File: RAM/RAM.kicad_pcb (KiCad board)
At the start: 2 copper layers, 138 x 63.8 mm, 52 parts, among them J1 Conn_01x02_Pin, J2 Conn_01x01_Pin, J3 Conn_01x02_Pin, J4 Conn_01x01_Pin, J5 Conn_01x05_Pin, J6 Conn_01x03_Pin, J7 Conn_01x03_Pin, J8 Conn_01x03_Pin, J9 Conn_01x10_Pin, U2 CD74HCT258E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

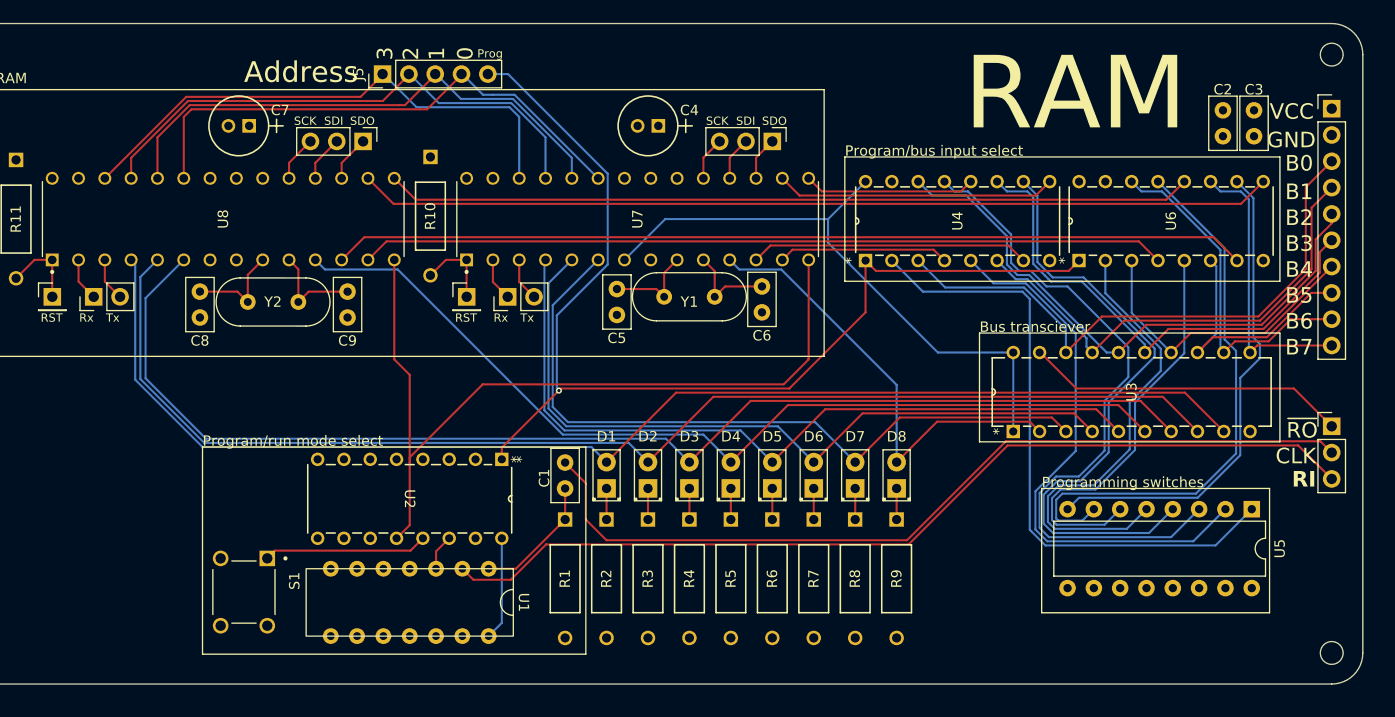
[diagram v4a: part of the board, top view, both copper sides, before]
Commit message: Updated RAM LED footprints
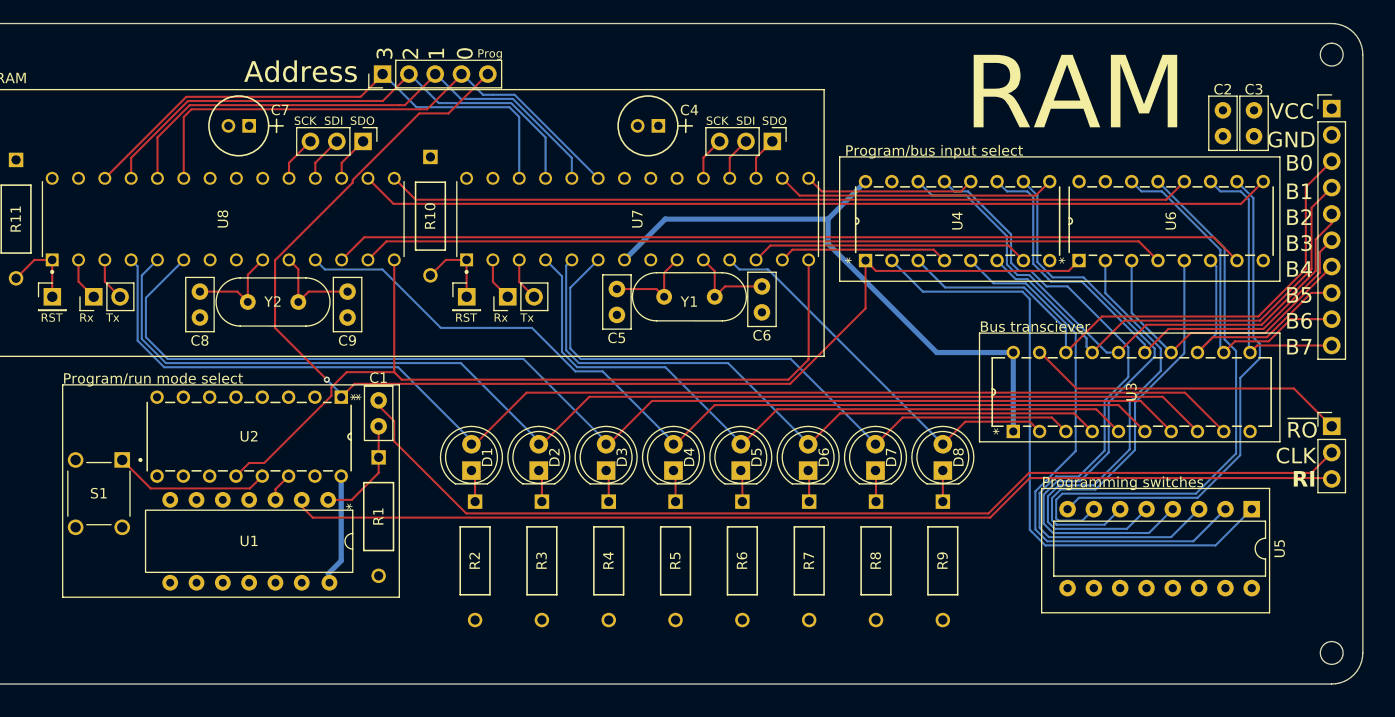
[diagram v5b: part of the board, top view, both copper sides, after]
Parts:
- D1, D2, D3, D4, D5, D6, D7, D8: footprint LED_THT:LED_D2.0mm_W4.8mm_H2.5mm_FlatTop -> LED_THT:LED_D5.0mm
- moved C1 19.0 mm to (161.0, 74.5)
- moved R1 19.0 mm to (161.0, 80.0)
- moved S1 16.9 mm to (134.0, 83.5)
- moved U2 16.6 mm to (139.6, 81.8)
- moved U1 16.6 mm to (148.5, 88.1)
- moved D1 13.2 mm to (170.0, 81.3)
- moved R2 12.8 mm to (170.3, 84.3)
- moved D2 10.7 mm to (176.5, 81.3)
- moved R3 10.4 mm to (176.8, 84.3)
- moved D3 8.22 mm to (183.0, 81.3)
- moved R4 7.98 mm to (183.2, 84.3)
- moved D4 5.80 mm to (189.5, 81.3)
- moved R5 5.61 mm to (189.7, 84.3)
- moved D8 4.78 mm to (215.5, 81.3)
- moved R9 4.78 mm to (215.5, 84.3)
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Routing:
- net /Program: track 106.7 -> 124.2 mm
- net /CLK: track 83.6 -> 99.9 mm
- net /Read in: track 91.1 -> 101.5 mm
- net /Data out 2: track 72.6 -> 65.4 mm
- net /Data out 1: track 70.1 -> 63.0 mm
- net /Data out 3: track 75.1 -> 69.2 mm
- net /Data out 0: track 44.4 -> 38.6 mm
- net /Data out 6: track 121.5 -> 117.7 mm
- net /Data out 5: track 119.0 -> 115.2 mm
- net /Data out 7: track 124.4 -> 120.7 mm
- net /Data out 4: track 91.5 -> 90.1 mm
- net Net-(U1-1A): track 12.3 -> 11.1 mm
- net /AtmegaRamEmulatorA/~{WE}: track 80.6 -> 81.5 mm
- net Net-(U2-4A): track 15.8 -> 15.2 mm

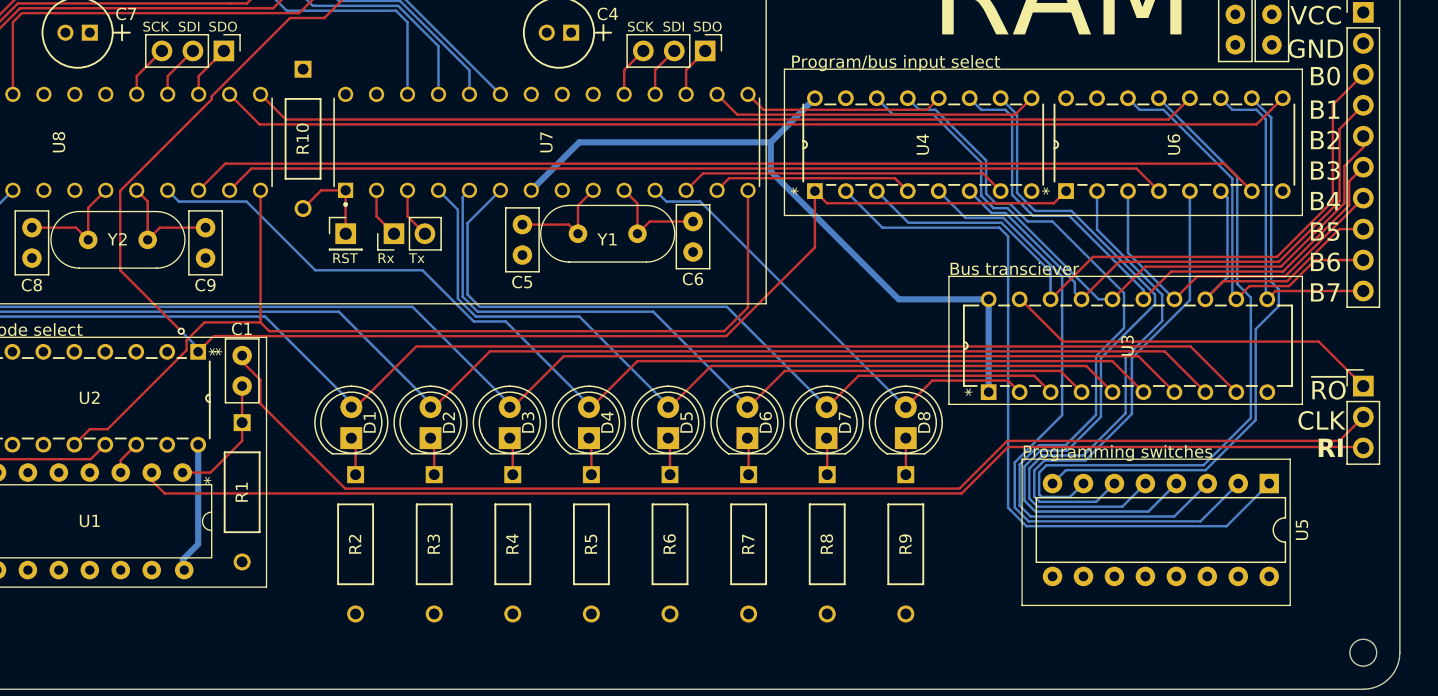
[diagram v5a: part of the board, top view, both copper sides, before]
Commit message: Reduced RAM layout
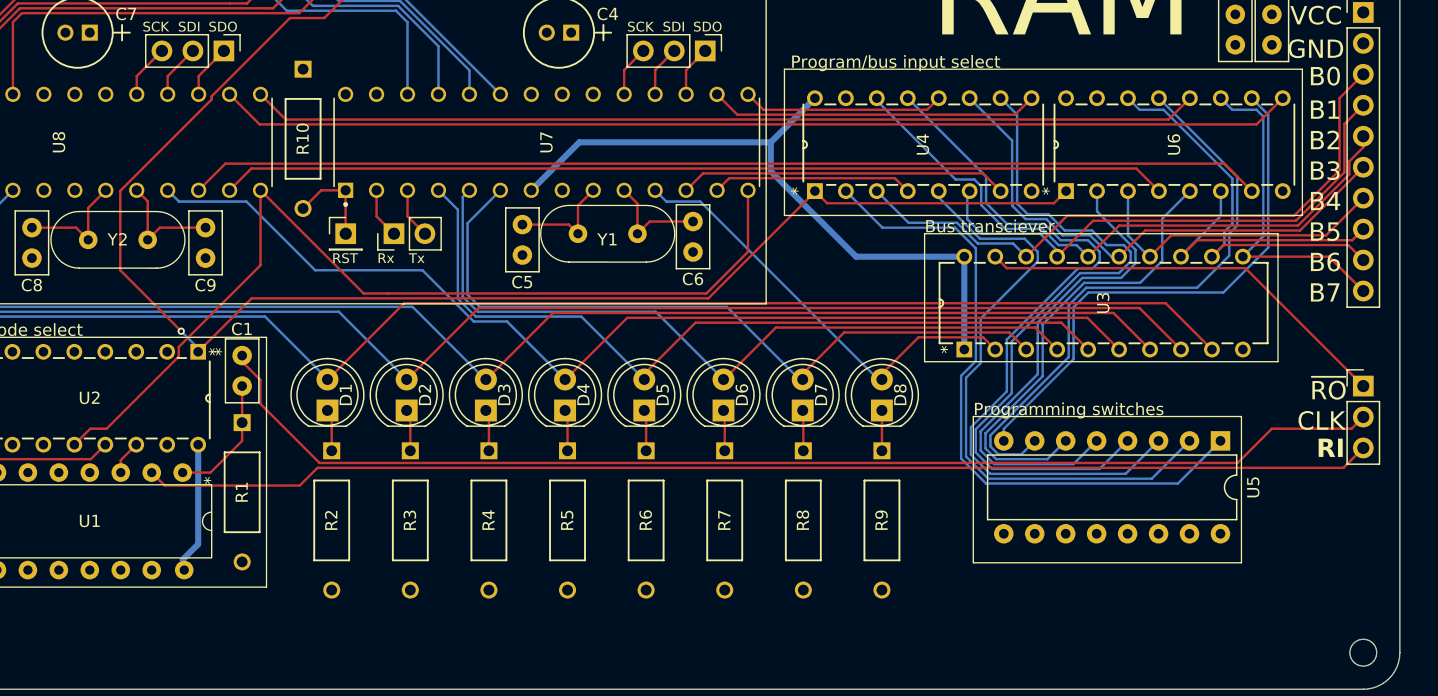
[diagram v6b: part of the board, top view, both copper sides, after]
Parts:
- moved U5 5.32 mm to (241.3, 81.5)
- moved U3 4.03 mm to (243.1, 66.4)
- moved D1 3.00 mm to (168.0, 79.0)
- moved D2 3.00 mm to (174.5, 79.0)
- moved D3 3.00 mm to (181.0, 79.0)
- moved D4 3.00 mm to (187.5, 79.0)
- moved D5 3.00 mm to (194.0, 79.0)
- moved D6 3.00 mm to (200.5, 79.0)
- moved D7 3.00 mm to (207.0, 79.0)
- moved D8 3.00 mm to (213.5, 79.0)
- moved R2 2.77 mm to (168.3, 82.3)
- moved R4 2.77 mm to (181.2, 82.3)
- moved R5 2.77 mm to (187.7, 82.3)
- moved R6 2.77 mm to (194.2, 82.3)
- moved R7 2.77 mm to (200.6, 82.3)
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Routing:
- net /Prog 0: track 60.6 -> 53.9 mm
- net /Bus 0: track 57.2 -> 51.8 mm
- net /Prog 6: track 54.6 -> 49.3 mm
- net /Bus 3: track 49.0 -> 43.8 mm
- net /Bus 2: track 56.2 -> 51.6 mm
- net /Prog 4: track 44.5 -> 40.5 mm
- net /Prog 2: track 65.1 -> 61.1 mm
- net /Bus 4: track 29.4 -> 25.7 mm
- net /Prog 1: track 53.7 -> 50.1 mm
- net /AtmegaRamEmulatorA/~{WE}: track 81.5 -> 78.0 mm
- net /~Read out: track 31.1 -> 34.6 mm
- net +5V: track 68.6 -> 65.1 mm
- net /Prog 7: track 46.9 -> 44.2 mm
- net /Program: track 124.2 -> 121.5 mm
- net /Bus 1: track 46.5 -> 43.9 mm
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
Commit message: RAM cosmetic updates
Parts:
- moved REF** 7.81 mm to (126.0, 92.9)
- moved S1 6.37 mm to (131.2, 77.8), turned to 180 degrees
- moved REF** 6.00 mm to (253.0, 92.9)
- moved REF** 5.01 mm to (126.0, 40.8)
- moved J5 0.25 mm to (161.4, 42.8)
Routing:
- net Net-(U2-4A): track 15.2 -> 17.4 mm
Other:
- board size 138 x 63.8 mm -> 133 x 58.1 mm
- board text added: "4"
- board text added: "5"
- board text added: "6"
- board text added: "7"

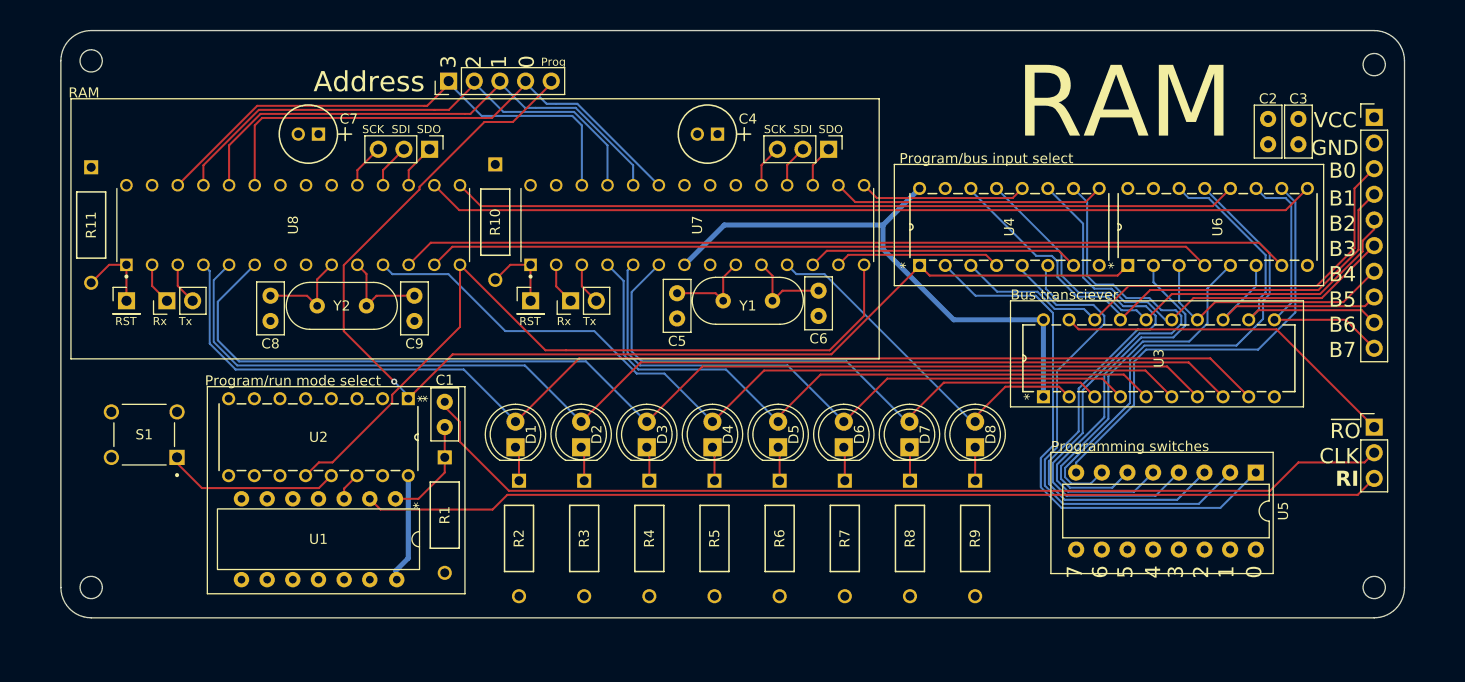
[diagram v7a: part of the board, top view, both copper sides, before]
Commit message: Added pullup resistors to the programming switches
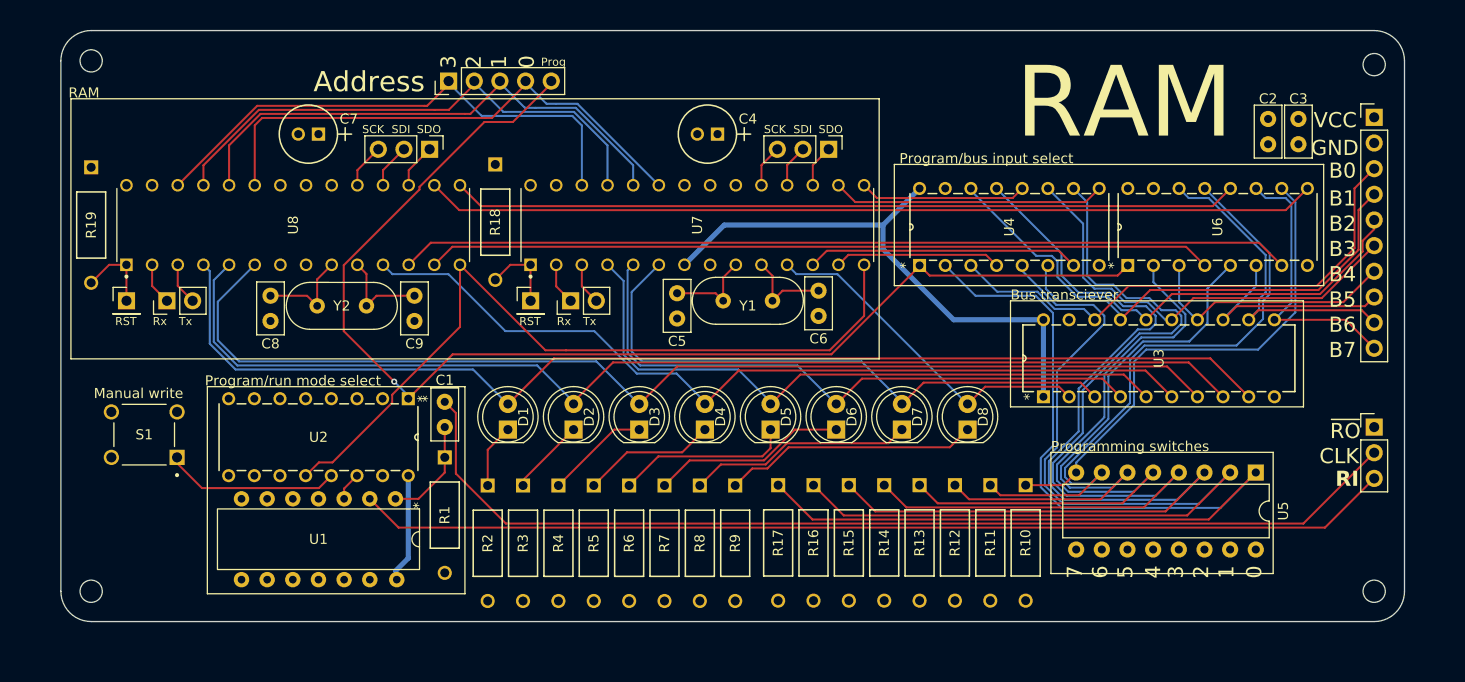
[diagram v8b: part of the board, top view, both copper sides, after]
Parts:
- added R10: 1k, _DownloadFootprints:CF_series_Resistors_THT, F.Cu at (218.5, 82.8)
- added R11: 1k, _DownloadFootprints:CF_series_Resistors_THT, F.Cu at (215.0, 82.8)
- added R12: 1k, _DownloadFootprints:CF_series_Resistors_THT, F.Cu at (211.5, 82.8)
- added R13: 1k, _DownloadFootprints:CF_series_Resistors_THT, F.Cu at (208.0, 82.8)
- added R14: 1k, _DownloadFootprints:CF_series_Resistors_THT, F.Cu at (204.5, 82.8)
- added R15: 1k, _DownloadFootprints:CF_series_Resistors_THT, F.Cu at (201.0, 82.8)
- added R16: 1k, _DownloadFootprints:CF_series_Resistors_THT, F.Cu at (197.5, 82.8)
- added R17: 1k, _DownloadFootprints:CF_series_Resistors_THT, F.Cu at (194.0, 82.8)
- moved R9 23.8 mm to (189.8, 82.8)
- moved R8 20.8 mm to (186.2, 82.8)
- moved R7 17.9 mm to (182.8, 82.8)
- moved R6 14.9 mm to (179.2, 82.8)
- moved R5 12.0 mm to (175.8, 82.8)
- moved R4 9.01 mm to (172.2, 82.8)
- moved R3 6.07 mm to (168.8, 82.8)
- moved R2 3.14 mm to (165.2, 82.8)
- moved D1 1.90 mm to (167.2, 77.2)
- moved D2 1.90 mm to (173.8, 77.2)
- moved D3 1.90 mm to (180.2, 77.2)
- moved D4 1.90 mm to (186.8, 77.2)
- moved D5 1.90 mm to (193.2, 77.2)
- moved D6 1.90 mm to (199.8, 77.2)
- moved D7 1.90 mm to (206.2, 77.2)
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- renumbered R10 to R18, R11 to R19
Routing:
- net /Prog 0: track 53.9 -> 104.6 mm
- net /Prog 1: track 50.1 -> 94.4 mm
- net /Prog 2: track 61.1 -> 99.0 mm
- net /~Read out: track 34.6 -> 0.00 mm
- net /Prog 3: track 57.7 -> 89.2 mm
- net /Prog 4: track 40.5 -> 65.6 mm
- net Net-(D8-K): track 3.31 -> 25.3 mm
- net Net-(D7-K): track 3.00 -> 22.3 mm
- net /Prog 5: track 38.3 -> 57.1 mm
- net Net-(D6-K): track 3.00 -> 19.3 mm
- net Net-(D5-K): track 3.00 -> 17.4 mm
- net /Prog 6: track 49.3 -> 61.7 mm
- net Net-(D4-K): track 3.00 -> 13.3 mm
- net Net-(D3-K): track 3.00 -> 10.3 mm
- net /Prog 7: track 44.2 -> 49.7 mm
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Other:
- board size 133 x 58.1 mm -> 133 x 58.5 mm
- board text added: "Manual write"
